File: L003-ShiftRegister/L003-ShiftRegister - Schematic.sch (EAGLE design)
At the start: 30 parts, among them IC1 4015N

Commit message: Update everything to use 1n60p Schottky diodes
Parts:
- D10, D11, D12, D13, D14, D15, D2, D3, D4, D5, D6, D7, D8, D9: value 1N5817 -> 1N60P
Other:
- note added: "close to power pins"
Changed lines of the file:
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@@
 <part name="R4" library="resistor" deviceset="R-US_" device="VMTA55" value="4.7K"/>
 <part name="D1" library="led" deviceset="SFH482" device="" value="LED"/>
-<part name="D2" library="diode" deviceset="1N581*" device="" technology="7-B" value="1N5817"/>
-<part name="D3" library="diode" deviceset="1N581*" device="" technology="7-B" value="1N5817"/>
+<part name="D2" library="diode" deviceset="1N581*" device="" technology="7-B" value="1N60P"/>
+<part name="D3" library="diode" deviceset="1N581*" device="" technology="7-B" value="1N60P"/>
 <part name="R5" library="resistor" deviceset="R-US_" device="VMTA55" value="1K"/>
 <part name="C2" library="rcl" deviceset="CPOL-US" device="E2.5-6" value="0.1~1uF"/>
@@
 <part name="R3" library="resistor" deviceset="R-US_" device="VMTA55" value="1K"/>
 <part name="R8" library="resistor" deviceset="R-US_" device="VMTA55" value="1M"/>
-<part name="D4" library="diode" deviceset="1N581*" device="" technology="7-B" value="1N5817"/>
-<part name="D5" library="diode" deviceset="1N581*" device="" technology="7-B" value="1N5817"/>
+<part name="D4" library="diode" deviceset="1N581*" device="" technology="7-B" value="1N60P"/>
+<part name="D5" library="diode" deviceset="1N581*" device="" technology="7-B" value="1N60P"/>
 <part name="R1" library="resistor" deviceset="R-US_" device="VMTA55" value="1K"/>
 <part name="R2" library="resistor" deviceset="R-US_" device="VMTA55" value="1M"/>
-<part name="D6" library="diode" deviceset="1N581*" device="" technology="7-B" value="1N5817"/>
-<part name="D7" library="diode" deviceset="1N581*" device="" technology="7-B" value="1N5817"/>
+<part name="D6" library="diode" deviceset="1N581*" device="" technology="7-B" value="1N60P"/>
+<part name="D7" library="diode" deviceset="1N581*" device="" technology="7-B" value="1N60P"/>
 <part name="R6" library="resistor" deviceset="R-US_" device="VMTA55" value="1K"/>
 <part name="R7" library="resistor" deviceset="R-US_" device="VMTA55" value="1M"/>
-<part name="D8" library="diode" deviceset="1N581*" device="" technology="7-B" value="1N5817"/>
-<part name="D9" library="diode" deviceset="1N581*" device="" technology="7-B" value="1N5817"/>
-<part name="D10" library="diode" deviceset="1N581*" device="" technology="7-B" value="1N5817"/>
-<part name="D11" library="diode" deviceset="1N581*" device="" technology="7-B" value="1N5817"/>
+<part name="D8" library="diode" deviceset="1N581*" device="" technology="7-B" value="1N60P"/>
+<part name="D9" library="diode" deviceset="1N581*" device="" technology="7-B" value="1N60P"/>
+<part name="D10" library="diode" deviceset="1N581*" device="" technology="7-B" value="1N60P"/>
+<part name="D11" library="diode" deviceset="1N581*" device="" technology="7-B" value="1N60P"/>
 <part name="R9" library="resistor" deviceset="R-US_" device="VMTA55" value="1K"/>
-<part name="D12" library="diode" deviceset="1N581*" device="" technology="7-B" value="1N5817"/>
-<part name="D13" library="diode" deviceset="1N581*" device="" technology="7-B" value="1N5817"/>
+<part name="D12" library="diode" deviceset="1N581*" device="" technology="7-B" value="1N60P"/>
+<part name="D13" library="diode" deviceset="1N581*" device="" technology="7-B" value="1N60P"/>
 <part name="R10" library="resistor" deviceset="R-US_" device="VMTA55" value="1K"/>
-<part name="D14" library="diode" deviceset="1N581*" device="" technology="7-B" value="1N5817"/>
-<part name="D15" library="diode" deviceset="1N581*" device="" technology="7-B" value="1N5817"/>
+<part name="D14" library="diode" deviceset="1N581*" device="" technology="7-B" value="1N60P"/>
+<part name="D15" library="diode" deviceset="1N581*" device="" technology="7-B" value="1N60P"/>
 <part name="R11" library="resistor" deviceset="R-US_" device="VMTA55" value="1K"/>
 <part name="R12" library="resistor" deviceset="R-US_" device="VMTA55" value="4.7K"/>
@@
 <plain>
 <text x="22.86" y="53.34" size="1.778" layer="91">this x2</text>
+<text x="-48.26" y="35.56" size="1.778" layer="91">close to power pins</text>
 </plain>
 <instances>

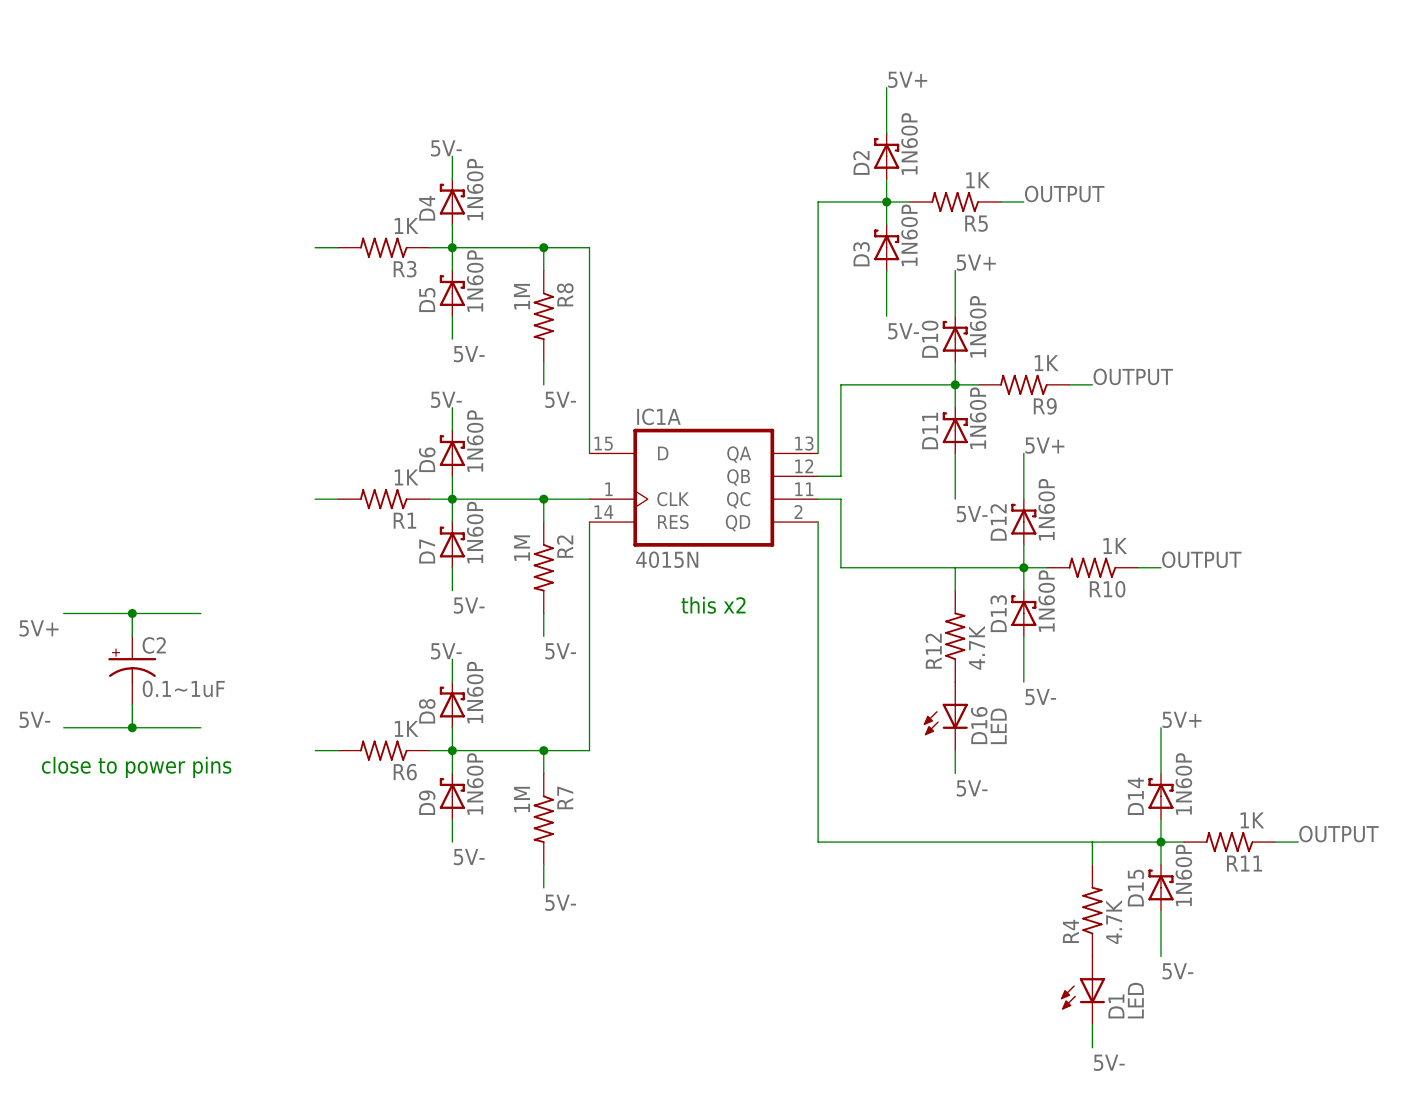
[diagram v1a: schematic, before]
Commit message: 10k r on outputs
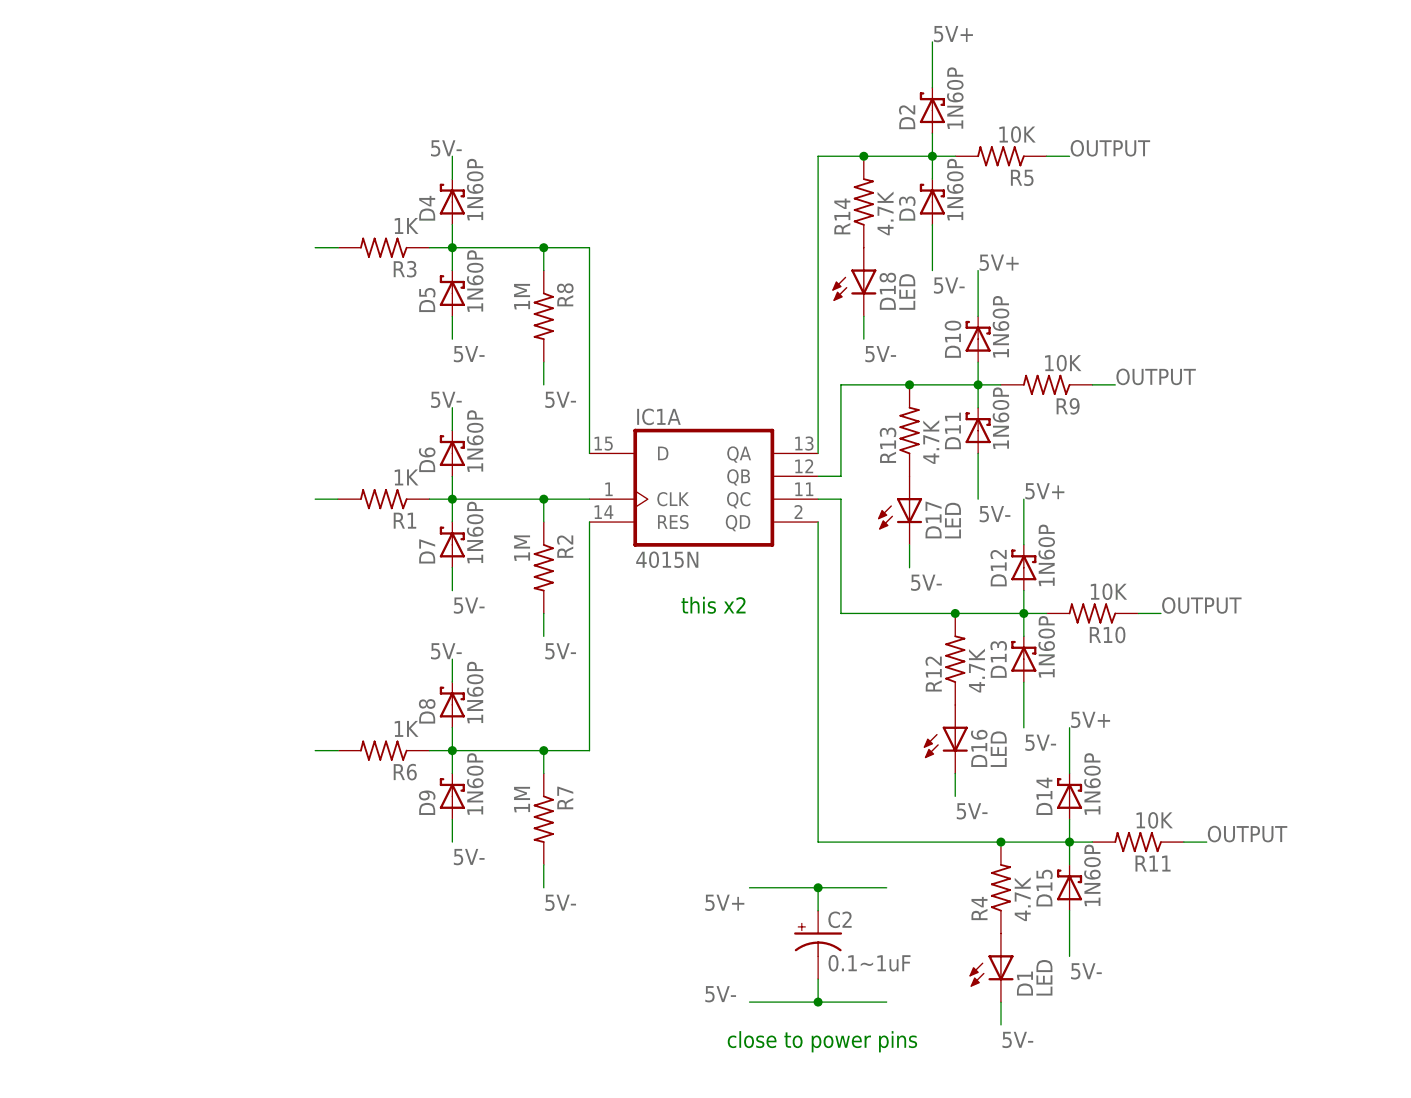
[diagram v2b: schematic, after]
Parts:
- added D17, D18: LED, led:SFH482
- added R13, R14: 4.7K, resistor:R-US_VMTA55
- R10, R11, R5, R9: value 1K -> 10K
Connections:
- net 5V-: now also D17.C, D18.C
- net N$10: now also R13.2
- net N$11: now also R12.2
- net N$12: now also R4.2
- net N$13: now also D18.A, R14.1; no longer R12.2
- net N$4: now also R14.2
- net N$5: now also D17.A, R13.1; no longer R4.2
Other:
- moved on the sheet: C2, D1, D10, D11, D12, D13, D14, D15, D16, D2, D3, R10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
